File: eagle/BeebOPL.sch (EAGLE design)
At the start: 31 parts, among them IC1 LM324N, IC2 YM3014B, IC3 74LS00N, IC4 74LS27N, IC5 74LS02N, IC6 YM3812, IC7 74LS04N, J1 1 MHz Bus, J2 Feed-through, J3 3.5mm Jack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

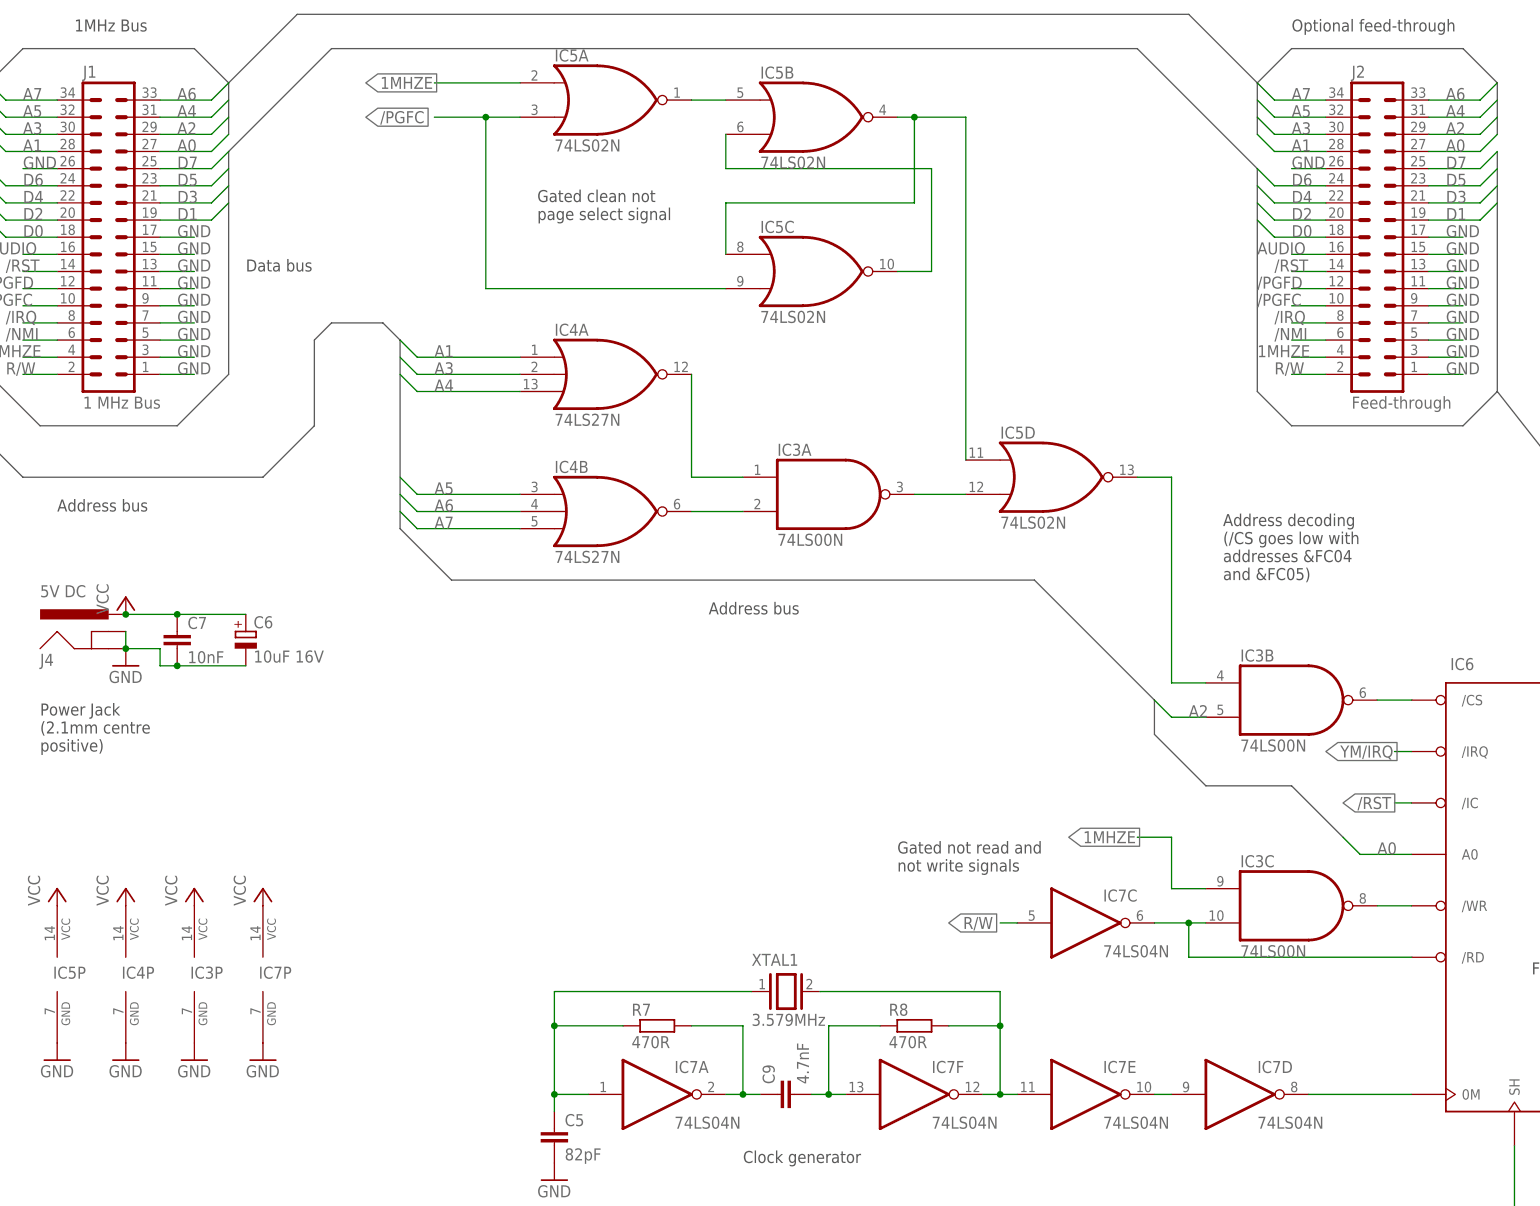
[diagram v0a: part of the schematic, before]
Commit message: Replaced 74LS27 with 74HCT688
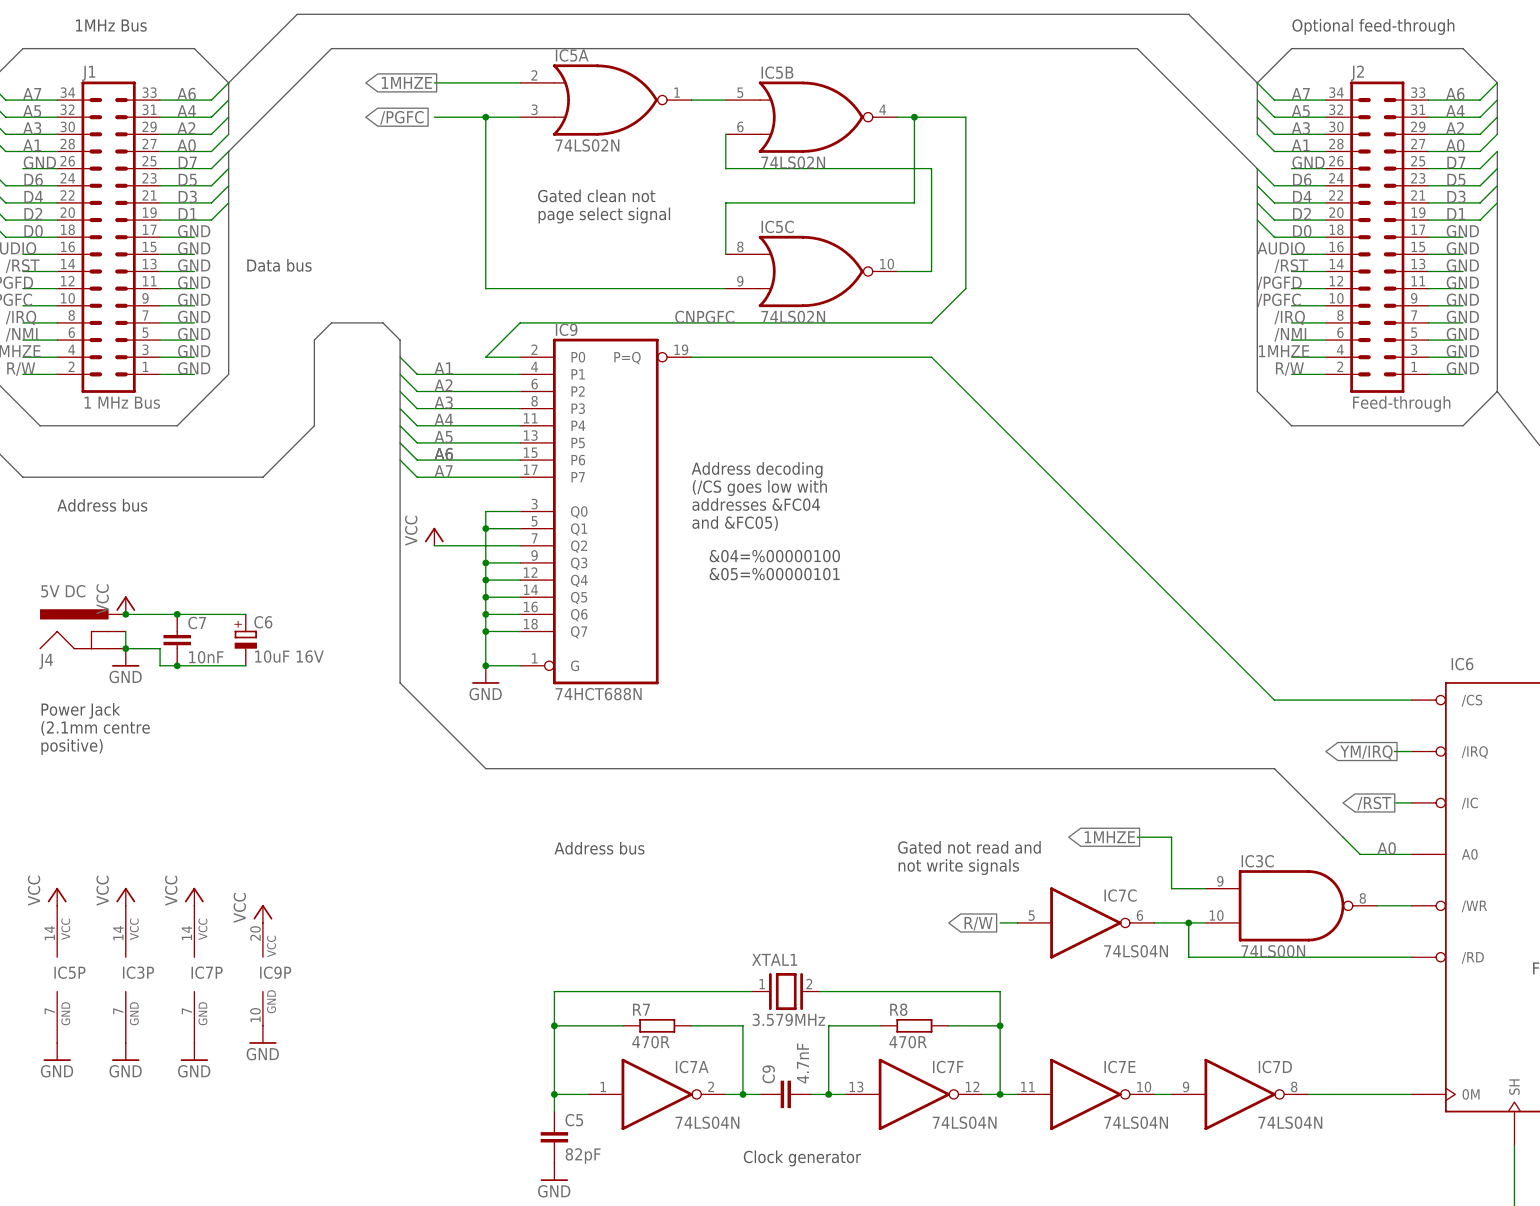
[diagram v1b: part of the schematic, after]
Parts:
- removed IC4: 74LS27N, 74xx-us:74LS27N
- added IC9: 74HCT688N, 74xx-eu:74HCT688N
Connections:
- removed net N$14: IC3A.O, IC5D.I1
- removed net N$2: IC3A.I0, IC4A.O
- removed net N$23: IC3B.I0, IC5D.O
- removed net N$3: IC3A.I1, IC4B.O
- net A1: now also IC9A.P1; no longer IC4A.I0
- net A2: now also IC9A.P2; no longer IC3B.I1
- net A3: now also IC9A.P3; no longer IC4A.I1
- net A4: now also IC9A.P4; no longer IC4A.I2
- net A5: now also IC9A.P5; no longer IC4B.I0
- net A6: now also IC9A.P6; no longer IC4B.I1
- net A7: now also IC9A.P7; no longer IC4B.I2
- net CNPGFC: now also IC9A.P0; no longer IC5D.I0
- net GND: now also IC9A.G, IC9A.Q0, IC9A.Q1, IC9A.Q3, IC9A.Q4, IC9A.Q5, IC9A.Q6, IC9A.Q7, IC9P.GND; no longer IC4P.GND
- net N$30: now also IC9A.P=Q; no longer IC3B.O
- net VCC: now also IC9A.Q2, IC9P.VCC; no longer IC4P.VCC
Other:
- note added: "&04=%00000100 &05=%00000101"
- moved on the sheet: IC3P, IC7P

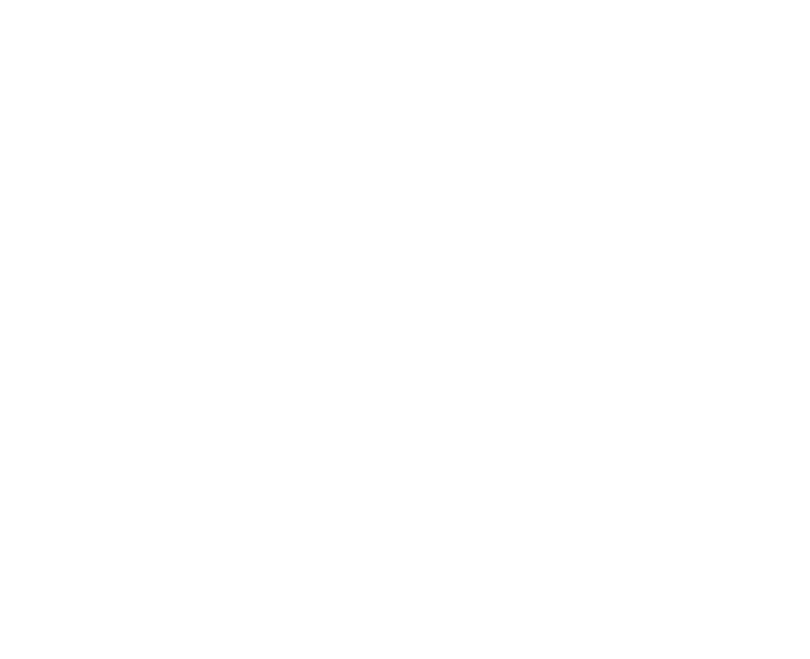
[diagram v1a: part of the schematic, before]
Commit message: Added mounting holes
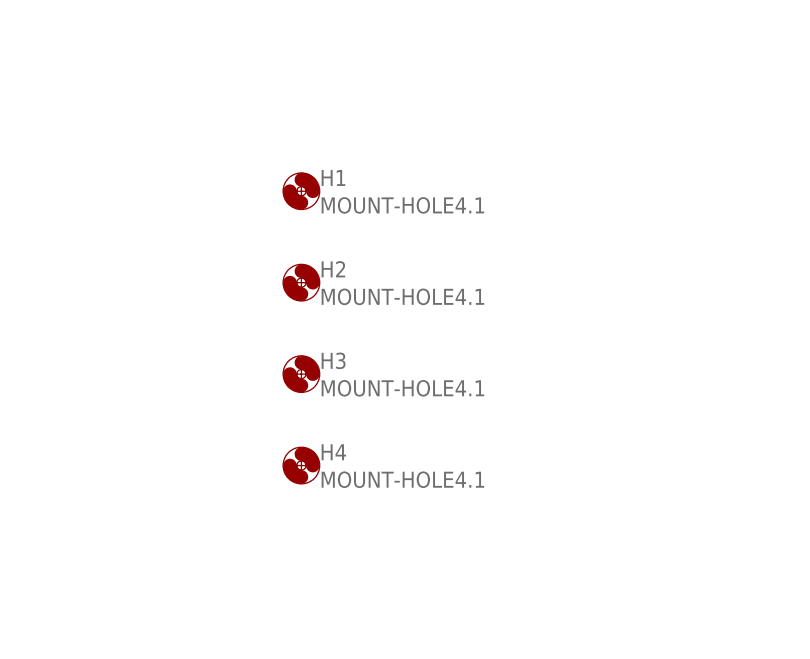
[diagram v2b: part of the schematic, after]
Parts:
- added H1, H2, H3, H4: MOUNT-HOLE4.1, holes:MOUNT-HOLE4.1
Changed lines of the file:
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@@
 <part name="P+10" library="supply1" deviceset="VCC" device=""/>
 <part name="GND16" library="supply1" deviceset="GND" device=""/>
+<part name="H1" library="holes" deviceset="MOUNT-HOLE" device="4.1"/>
+<part name="H2" library="holes" deviceset="MOUNT-HOLE" device="4.1"/>
+<part name="H3" library="holes" deviceset="MOUNT-HOLE" device="4.1"/>
+<part name="H4" library="holes" deviceset="MOUNT-HOLE" device="4.1"/>
 </parts>
 <sheets>
@@
 <text x="-76.2" y="66.04" size="1.778" layer="97">&amp;04=%00000100
 &amp;05=%00000101</text>
-<frame x1="-203.2" y1="-127" x2="195.58" y2="170.18" columns="8" rows="5" layer="91"/>
 </plain>
 <instances>
@@
 <instance part="P+10" gate="VCC" x="-142.24" y="17.78"/>
 <instance part="GND16" gate="1" x="-142.24" y="-2.54"/>
+<instance part="H1" gate="G$1" x="134.62" y="127"/>
+<instance part="H2" gate="G$1" x="134.62" y="116.84"/>
+<instance part="H3" gate="G$1" x="134.62" y="106.68"/>
+<instance part="H4" gate="G$1" x="134.62" y="96.52"/>
 </instances>
 <busses>
